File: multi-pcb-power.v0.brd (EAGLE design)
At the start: 72.1 x 32.7 mm, 24 parts, among them Q5 TIP136, T2 BC618, X1 2.52B-ZR, X2 2.52B-ZR, X3 2.52B-ZR, X4 2.54B-ZR

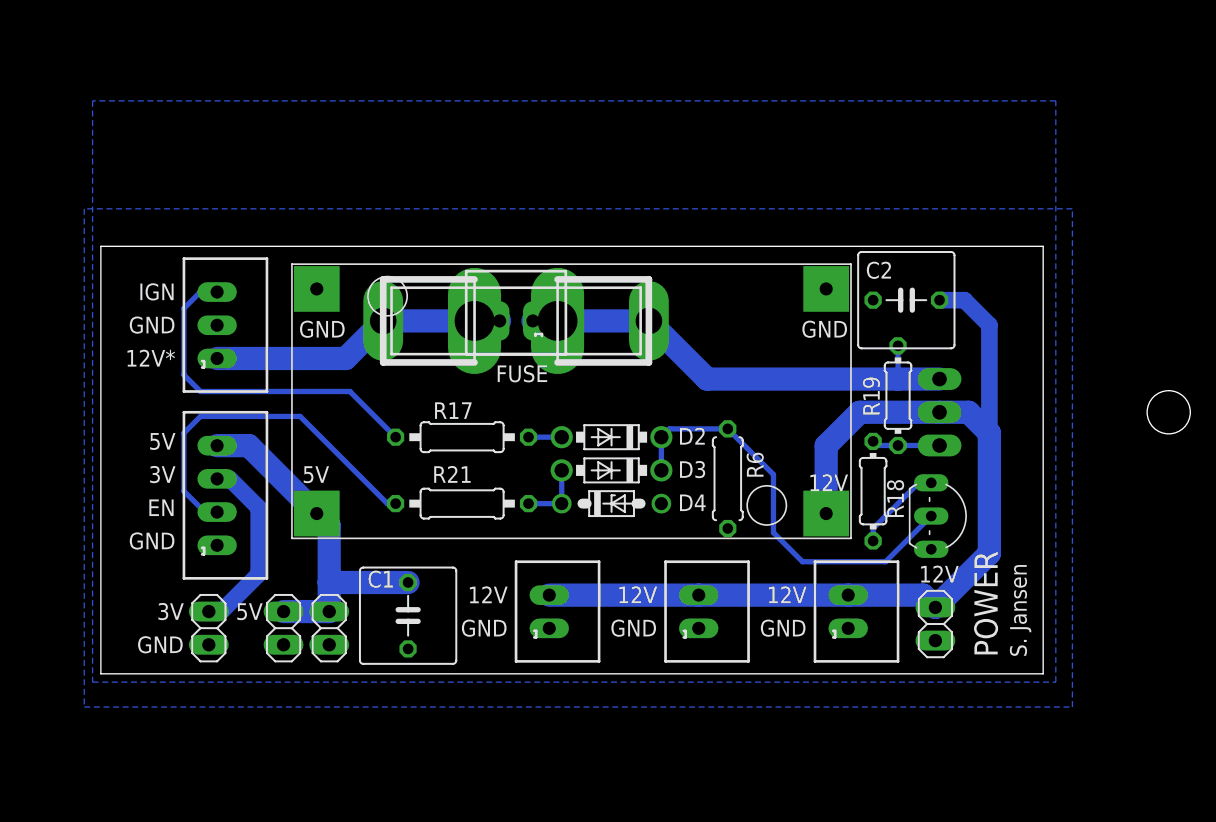
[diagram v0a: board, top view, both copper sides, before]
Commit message: Fixed PSU and fuse footprints. Also updated layout and added buffer capacitors.
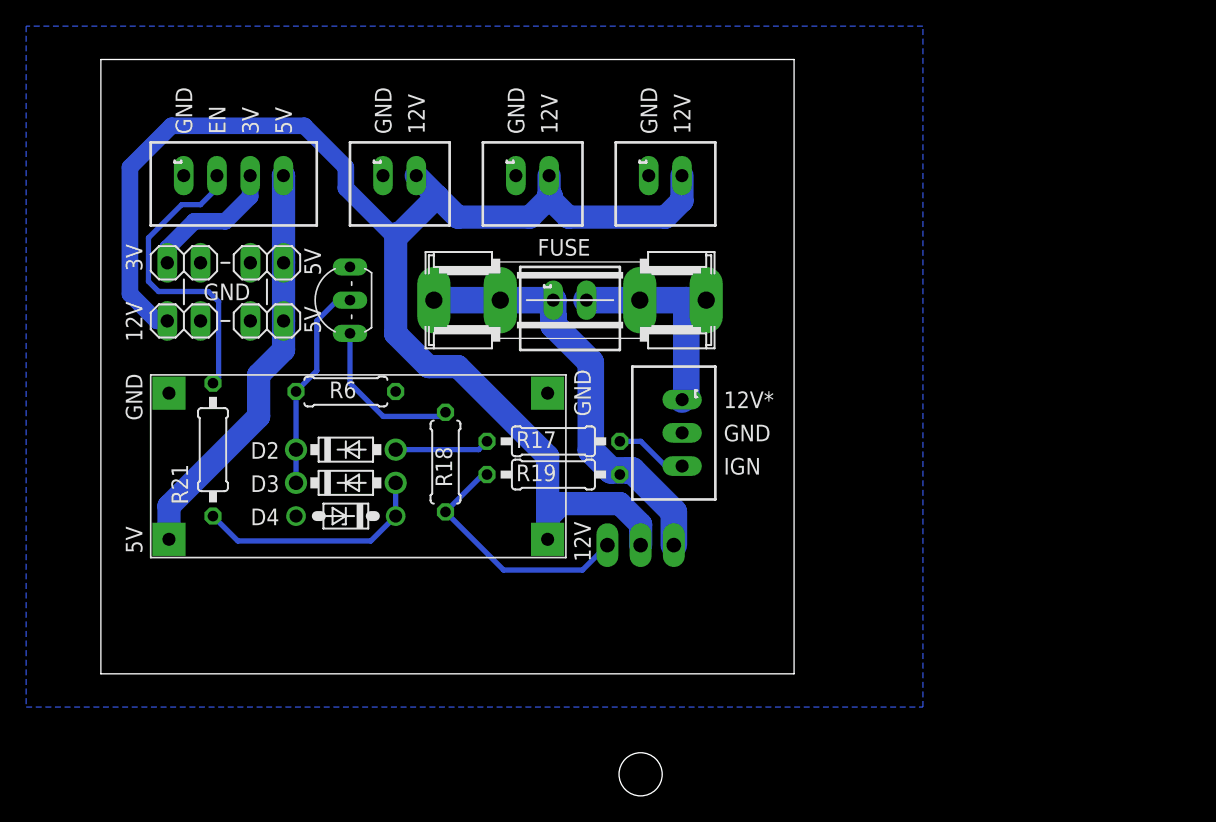
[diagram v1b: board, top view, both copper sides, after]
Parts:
- removed C1, C2: (no value), rcl:C050-075X075
- removed U$1: FUSE, samuel:FB-5X20
- added F1: 2A, fuse:SHK20L
- R18: device rcl:0204/7 -> rcl:0207/7
- R19: device rcl:0204/7 -> rcl:0207/10
- U$4: device samuel:LM2596S -> PSU:LM2596S
- moved JP_PWR_12V 62.0 mm to (6.35, 27.0), turned to 180 degrees
- moved T2 49.8 mm to (17.8, 28.6), turned to 90 degrees
- moved PWR 36.5 mm to (44.5, 18.4), turned to 270 degrees
- moved X1 36.1 mm to (43.2, 38.1), turned to 0 degrees
- moved X3 35.7 mm to (33.0, 38.1), turned to 0 degrees
- moved X2 35.2 mm to (22.9, 38.1), turned to 0 degrees
- moved Q5 33.6 mm to (41.3, 3.49), turned to 180 degrees
- moved R18 32.8 mm to (26.4, 16.2), turned to 90 degrees
- moved R6 30.0 mm to (18.7, 21.6), turned to 180 degrees
- moved JP_PWR_3V3 28.0 mm to (6.35, 31.4), turned to 180 degrees
- moved JP_PWR_5V_2 28.0 mm to (12.7, 31.4), turned to 0 degrees
- moved R19 27.0 mm to (34.6, 15.2), turned to 0 degrees
- moved X4 24.5 mm to (10.2, 38.1), turned to 0 degrees
- moved JP_PWR_5V_1 24.0 mm to (12.7, 27.0), turned to 0 degrees
- moved D2 20.3 mm to (18.7, 17.1), turned to 0 degrees
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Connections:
- net +12V: now also F1.2A; no longer U$1.P$3, U$1.P$4
- net +5V: no longer C1.1
- net GND: no longer C1.2, C2.2
- net N$21: now also F1.1A; no longer U$1.P$1, U$1.P$2
- net PWR_IN+: no longer C2.1
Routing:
- net PWR_IN+: track 77.2 -> 111.8 mm
- net IGNITION: track 26.3 -> 5.55 mm
- net N$5: track 31.7 -> 16.2 mm
- net N$14: track 5.21 -> 19.4 mm
- net N$11: track 5.08 -> 18.1 mm
- net +12V: track 22.8 -> 16.9 mm
- net N$15: track 6.84 -> 12.3 mm
- net N$12: track 2.54 -> 7.25 mm
- net +5V: track 27.2 -> 31.4 mm
- net PWR_ENABLE: track 27.1 -> 23.5 mm
- net +3V3: track 14.2 -> 10.7 mm
- net N$21: track 35.5 -> 33.4 mm
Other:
- board size 72.1 x 32.7 mm -> 53 x 47 mm
- board text removed: "POWER"
- board text removed: "S. Jansen"
